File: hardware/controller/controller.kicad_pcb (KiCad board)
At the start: 4 copper layers, 59 x 47 mm, 50 parts, among them J1 Conn_01x02_Pin, J11 Barrel_Jack, J12 USB_C_Receptacle_USB2.0_14P, J2 Conn_01x02_Pin, J3 Conn_01x02_Pin, J5 Screw_Terminal_01x02, J6 Screw_Terminal_01x02, J7 Conn_01x04_Pin, J8 Conn_01x04_Pin, U1 ESP32-C3-MINI-1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

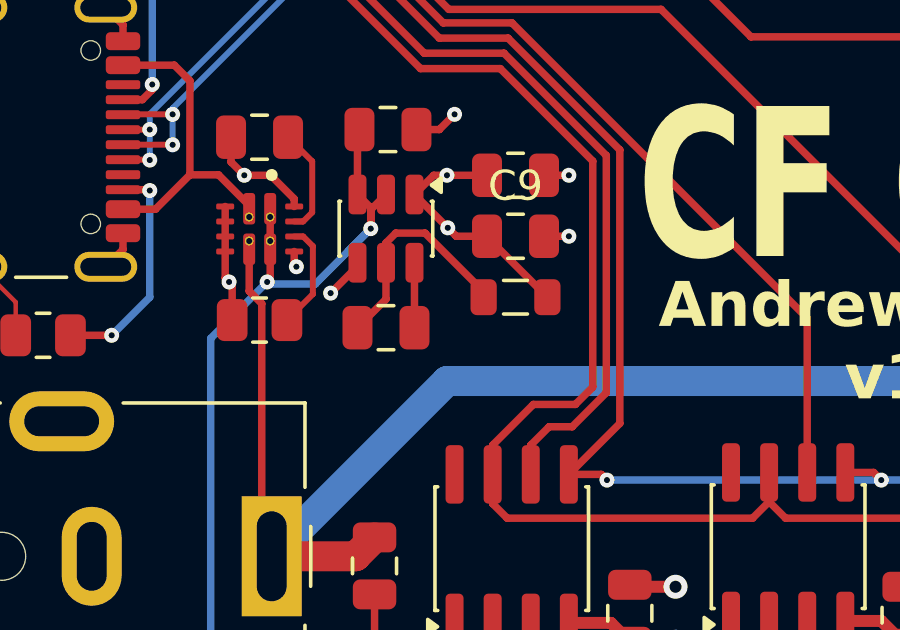
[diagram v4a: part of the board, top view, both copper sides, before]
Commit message: Update inductor to match regulator spec better
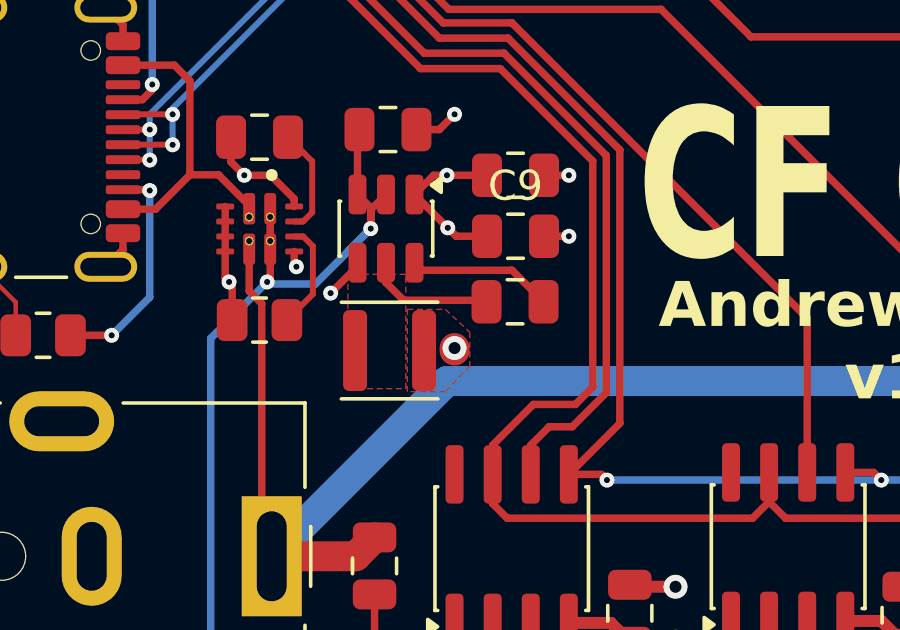
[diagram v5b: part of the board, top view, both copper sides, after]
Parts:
- L1: footprint Inductor_SMD:L_0805_2012Metric -> Inductor_SMD:L_APV_ANR3015
- moved L1 4.56 mm to (123.6, 97.3)
- moved C13 4.39 mm to (127.7, 95.7)
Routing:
- net Net-(U8-SW): track 7.60 -> 4.28 mm
- net +3V3: track 31.5 -> 28.8 mm, vias 10 -> 11
- net Net-(U8-BST): track 2.16 -> 4.84 mm
- added copper zone on F.Cu, net +3V3
- added copper zone on F.Cu, net Net-(U8-SW)
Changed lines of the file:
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@@
 	(footprint "Capacitor_SMD:C_0805_2012Metric"
 		(layer "F.Cu")
-		(at 123.444 96.52)
+		(at 127.7468 95.6564)
 		(descr "Capacitor SMD 0805 (2012 Metric), square (rectangular) end terminal, IPC-7351 nominal, (Body size source: IPC-SM-782 page 76, https://www.pcb-3d.com/wordpress/wp-content/uploads/ipc-sm-782a_amendment_1_and_2.pdf, https://docs.google.com/spreadsheets/d/1BsfQQcO9C6DZCsRaXUlFlo91Tg2WpOkGARC1WS5S8t0/edit?usp=sharing), generated with kicad-footprint-generator")
 		(tags "capacitor")
@@
 		)
 	)
-	(footprint "Inductor_SMD:L_0805_2012Metric"
+	(footprint "Inductor_SMD:L_APV_ANR3015"
 		(layer "F.Cu")
-		(at 127.762 95.504)
-		(descr "Inductor SMD 0805 (2012 Metric), square (rectangular) end terminal, IPC-7351 nominal, (Body size source: IPC-SM-782 page 80, https://www.pcb-3d.com/wordpress/wp-content/uploads/ipc-sm-782a_amendment_1_and_2.pdf), generated with kicad-footprint-generator")
-		(tags "inductor")
+		(at 123.564 97.282)
+		(descr "Inductor, APV, ANR3015, 3.0x3.0x1.5mm, (http://en.apvind.com/public/upload/20240407/3375c395e460caa8519b4d637d9113ce.pdf), generated with kicad-footprint-generator gen_inductor.py")
+		(tags "wirewound power shielded")
 		(property "Reference" "L1"
-			(at 0 -1.55 0)
+			(at 0 -2.45 0)
 			(layer "F.SilkS")
 			(hide yes)
@@
 		)
 		(property "Value" "3.9uH"
-			(at 0 1.55 0)
+			(at 0 2.45 0)
 			(layer "F.Fab")
 			(effects
@@
 			)
 		)
-		(property "LCSC" "C69486"
+		(property "LCSC" "C42429305"
 			(at 0 0 0)
 			(unlocked yes)
@@
 		(attr smd)
 		(fp_line
-			(start -0.399622 -0.56)
-			(end 0.399622 -0.56)
+			(start -1.61 -1.61)
+			(end 1.61 -1.61)
 			(stroke
 				(width 0.12)
@@
 		)
 		(fp_line
-			(start -0.399622 0.56)
-			(end 0.399622 0.56)
+			(start 1.61 1.61)
+			(end -1.61 1.61)
 			(stroke
 				(width 0.12)
@@
 		)
 		(fp_line
-			(start -1.75 -0.85)
-			(end 1.75 -0.85)
+			(start -1.8 -1.6)
+			(end -1.75 -1.6)
 			(stroke
 				(width 0.05)
@@
 		)
 		(fp_line
-			(start -1.75 0.85)
-			(end -1.75 -0.85)
+			(start -1.8 1.6)
+			(end -1.8 -1.6)
 			(stroke
 				(width 0.05)
@@
 		)
 		(fp_line
-			(start 1.75 -0.85)
-			(end 1.75 0.85)
+			(start -1.75 -1.75)
+			(end 1.75 -1.75)
 			(stroke
 				(width 0.05)
@@
 		)
 		(fp_line
-			(start 1.75 0.85)
-			(end -1.75 0.85)
+			(start -1.75 -1.6)
+			(end -1.75 -1.75)
 			(stroke
 				(width 0.05)
@@
 		)
 		(fp_line
-			(start -1 -0.45)
-			(end 1 -0.45)
+			(start -1.75 1.6)
+			(end -1.8 1.6)
 			(stroke
-				(width 0.1)
+				(width 0.05)
 				(type solid)
 			)
-			(layer "F.Fab")
+			(layer "F.CrtYd")
 		)
 		(fp_line
-			(start -1 0.45)
-			(end -1 -0.45)
+			(start -1.75 1.75)
+			(end -1.75 1.6)
 			(stroke
-				(width 0.1)
+				(width 0.05)
 				(type solid)
 			)
-			(layer "F.Fab")
+			(layer "F.CrtYd")
 		)
 		(fp_line
-			(start 1 -0.45)
-			(end 1 0.45)
+			(start 1.75 -1.75)
+			(end 1.75 -1.6)
 			(stroke
-				(width 0.1)
+				(width 0.05)
 				(type solid)
 			)
-			(layer "F.Fab")
+			(layer "F.CrtYd")
 		)
 		(fp_line
-			(start 1 0.45)
-			(end -1 0.45)
+			(start 1.75 -1.6)
+			(end 1.8 -1.6)
+			(stroke
+				(width 0.05)
+				(type solid)
+			)
+			(layer "F.CrtYd")
+		)
+		(fp_line
+			(start 1.75 1.6)
+			(end 1.75 1.75)
+			(stroke
+				(width 0.05)
+				(type solid)
+			)
+			(layer "F.CrtYd")
+		)
+		(fp_line
+			(start 1.75 1.75)
+			(end -1.75 1.75)
+			(stroke
+				(width 0.05)
+				(type solid)
+			)
+			(layer "F.CrtYd")
+		)
+		(fp_line
+			(start 1.8 -1.6)
+			(end 1.8 1.6)
+			(stroke
+				(width 0.05)
+				(type solid)
+			)
+			(layer "F.CrtYd")
+		)
+		(fp_line
+			(start 1.8 1.6)
+			(end 1.75 1.6)
+			(stroke
+				(width 0.05)
+				(type solid)
+			)
+			(layer "F.CrtYd")
+		)
+		(fp_rect
+			(start -1.5 -1.5)
+			(end 1.5 1.5)
 			(stroke
 				(width 0.1)
 				(type solid)
 			)
+			(fill no)
 			(layer "F.Fab")
 		)
@@
 			(effects
 				(font
-					(size 0.5 0.5)
-					(thickness 0.08)
+					(size 0.75 0.75)
+					(thickness 0.11)
 				)
 			)
 		)
 		(pad "1" smd roundrect
-			(at -1.0625 0)
-			(size 0.875 1.2)
+			(at -1.15 0)
+			(size 0.8 2.7)
 			(layers "F.Cu" "F.Mask" "F.Paste")
 			(roundrect_rratio 0.25)
@@
 		)
 		(pad "2" smd roundrect
-			(at 1.0625 0)
-			(size 0.875 1.2)
+			(at 1.15 0)
+			(size 0.8 2.7)
 			(layers "F.Cu" "F.Mask" "F.Paste")
 			(roundrect_rratio 0.25)
@@
 		)
 		(embedded_fonts no)
-		(model "${KICAD9_3DMODEL_DIR}/Inductor_SMD.3dshapes/L_0805_2012Metric.step"
+		(model "${KICAD9_3DMODEL_DIR}/Inductor_SMD.3dshapes/L_APV_ANR3015.step"
 			(offset
 				(xyz 0 0 0)
@@
 	)
 	(segment
-		(start 126.812 93.4915)
-		(end 128.8245 95.504)
-		(width 0.25)
-		(layer "F.Cu")
-		(net 21)
-	)
-	(segment
 		(start 126.812 93.472)
 		(end 126.812 93.4915)
@@
 		(net 21)
 	)
+	(segment
+		(start 125.73 97.282)
+		(end 125.73 97.198)
+		(width 1)
+		(layer "F.Cu")
+		(net 21)
+	)
 	(via
 		(at 110.998 78.486)
@@
 	)
 	(via
+		(at 125.73 97.198)
+		(size 0.8)
+		(drill 0.4)
+		(layers "F.Cu" "B.Cu")
+		(net 21)
+	)
+	(via
 		(at 152.146 106.934)
 		(size 0.8)
@@
 	)
 	(segment
-		(start 124.394 96.52)
+		(start 124.6439 94.6054)
 		(end 124.394 94.3555)
 		(width 0.25)
@@
 	)
 	(segment
-		(start 124.745322 93.367)
-		(end 123.770001 93.367)
-		(width 0.25)
-		(layer "F.Cu")
-		(net 56)
-	)
-	(segment
-		(start 122.494 96.52)
-		(end 123.444 95.57)
+		(start 127.6458 94.6054)
+		(end 124.6439 94.6054)
 		(width 0.25)
 		(layer "F.Cu")
-		(net 56)
+		(net 55)
 	)
 	(segment
-		(start 126.6995 95.504)
-		(end 126.6995 95.321178)
+		(start 128.6968 95.6564)
+		(end 127.6458 94.6054)
 		(width 0.25)
 		(layer "F.Cu")
-		(net 56)
+		(net 55)
 	)
 	(segment
-		(start 126.6995 95.321178)
-		(end 124.745322 93.367)
+		(start 126.7968 95.6564)
+		(end 126.7464 95.606)
 		(width 0.25)
 		(layer "F.Cu")
@@
 	)
 	(segment
-		(start 123.444 93.693001)
-		(end 123.444 94.3555)
+		(start 124.032001 95.606)
+		(end 123.444 95.017999)
 		(width 0.25)
 		(layer "F.Cu")
@@
 	)
 	(segment
-		(start 123.770001 93.367)
-		(end 123.444 93.693001)
+		(start 126.7464 95.606)
+		(end 124.032001 95.606)
 		(width 0.25)
 		(layer "F.Cu")
@@
 	)
 	(segment
-		(start 123.444 95.57)
+		(start 123.444 95.017999)
 		(end 123.444 94.3555)
 		(width 0.25)
@@
 	)
 	(zone
+		(net 21)
+		(net_name "+3V3")
+		(layer "F.Cu")
+		(hatch edge 0.5)
+		(priority 4)
+		(connect_pads yes
+			(clearance 0.5)
+		)
+		(min_thickness 0.25)
+		(filled_areas_thickness no)
+		(fill yes
+			(thermal_gap 0.5)
+			(thermal_bridge_width 0.5)
+		)
+		(polygon
+			(pts
+				(xy 124.1552 95.9104) (xy 125.4252 95.9104) (xy 126.238 96.6724) (xy 126.238 97.79) (xy 125.4252 98.6536)
+				(xy 124.1552 98.6536)
+			)
+		)
+	)
+	(zone
 		(net 18)
 		(net_name "GND")
@@
 			)
 		)
+	)
+	(zone
+		(net 56)
+		(net_name "Net-(U8-SW)")
+		(layer "F.Cu")
+		(hatch edge 0.5)
+		(priority 3)
+		(connect_pads yes
+			(clearance 0.5)
+		)
+		(min_thickness 0.25)
+		(filled_areas_thickness no)
+		(fill yes
+			(thermal_gap 0.5)
+			(thermal_bridge_width 0.5)
+		)
+		(polygon
+			(pts
+				(xy 123.19 94.742) (xy 122.174 94.742) (xy 122.174 96.012) (xy 122.174 98.552) (xy 124.1044 98.552)
+				(xy 124.1044 94.742)
+			)
+		)

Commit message: 1.1 production tweaks
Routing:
- net VBUS: track 33.1 -> 32.0 mm
- net GND: vias 47 -> 46
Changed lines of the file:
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@@
 			)
 		)
+		(property "FT Rotation Offset" "90"
+			(at 0 0 270)
+			(unlocked yes)
+			(layer "F.Fab")
+			(hide yes)
+			(effects
+				(font
+					(size 1 1)
+					(thickness 0.15)
+				)
+			)
+		)
 		(property ki_fp_filters "TSOT?23*")
 		(sheetname "/Power/")
@@
 			(at 0 -1.68 0)
 			(layer "F.SilkS")
+			(hide yes)
 			(effects
 				(font
@@
 	)
 	(via
-		(at 128.778 72.644)
-		(size 0.5)
-		(drill 0.2)
-		(layers "F.Cu" "B.Cu")
-		(net 18)
-	)
-	(via
 		(at 120.4575 94.488)
 		(size 0.5)
@@
 		(width 0.25)
 		(layer "B.Cu")
-		(net 45)
-	)
-	(segment
-		(start 122.174 93.98)
-		(end 122.936 93.218)
-		(width 0.25)
-		(layer "B.Cu")

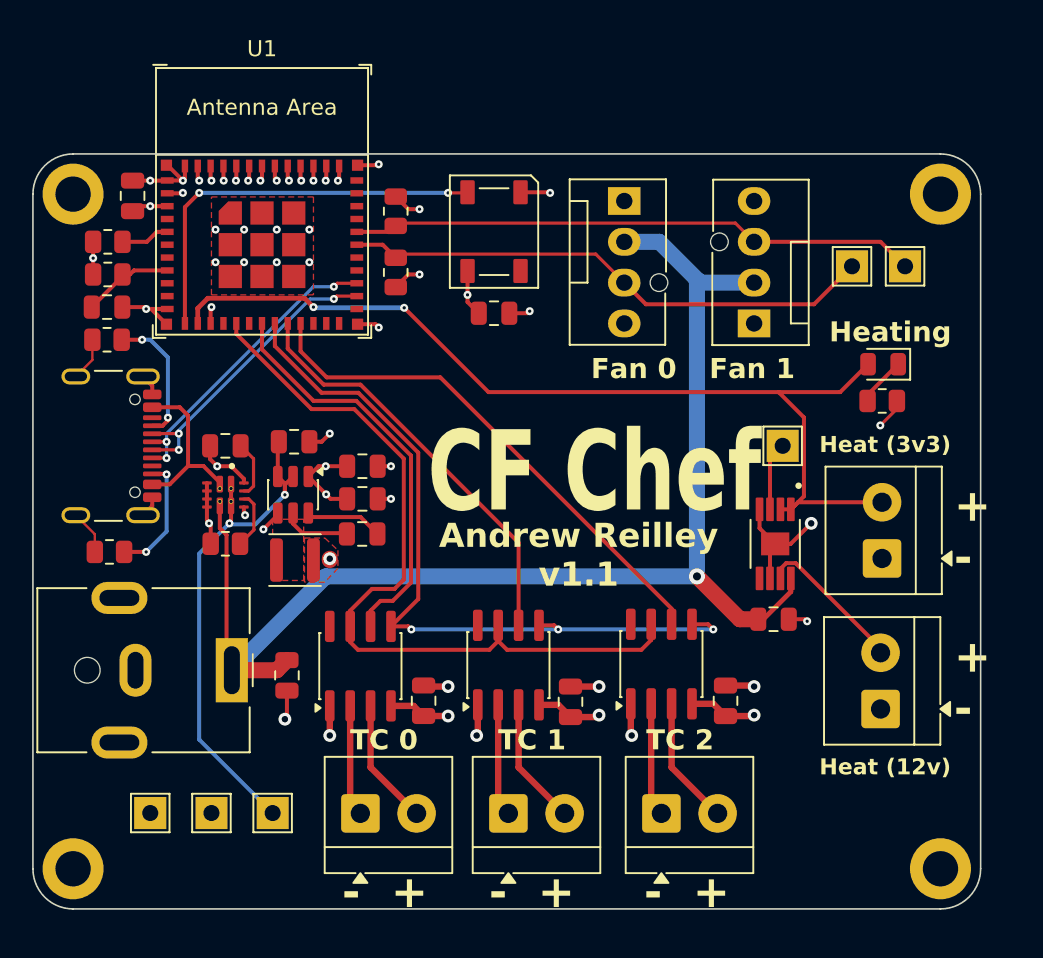
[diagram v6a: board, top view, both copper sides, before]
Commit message: Protect fan tach inputs
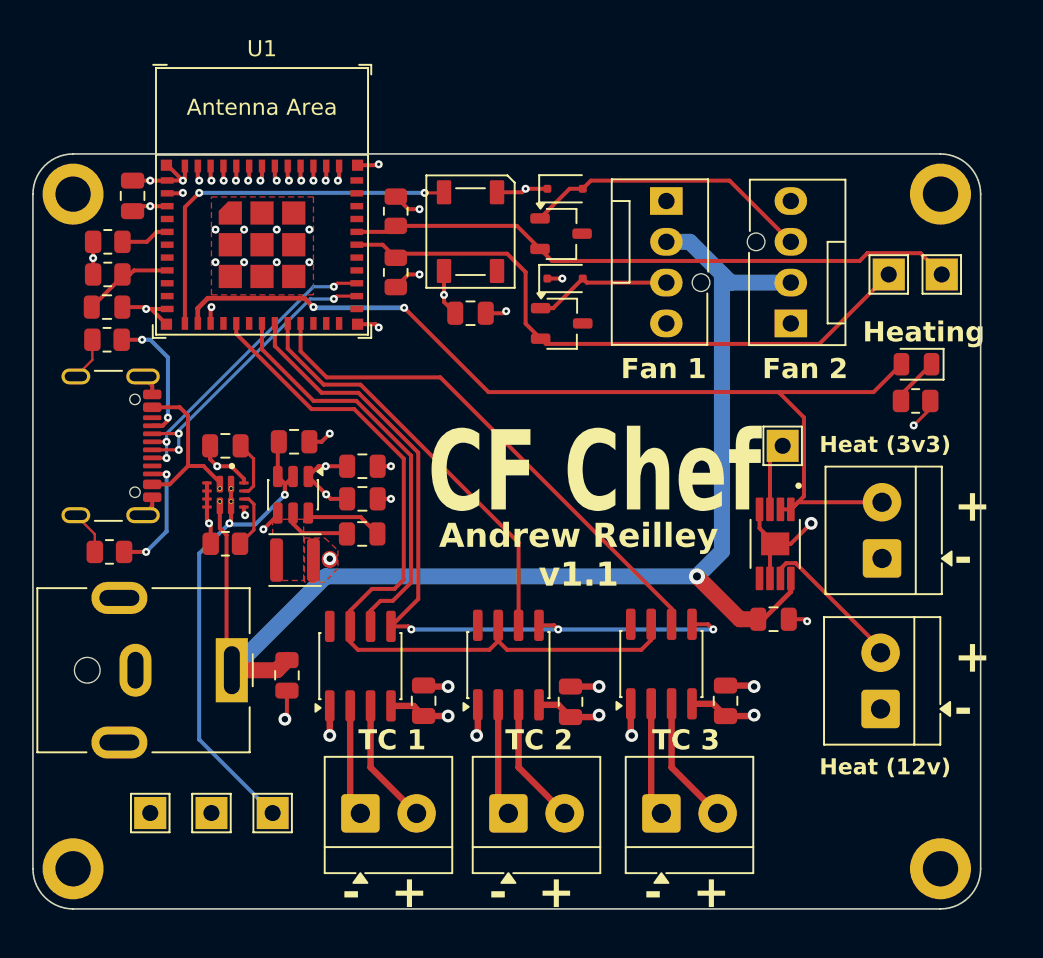
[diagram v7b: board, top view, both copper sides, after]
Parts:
- added D3: D, Package_TO_SOT_SMD:TSOT-23, F.Cu at (140.1, 77.0)
- added D4: D, Package_TO_SOT_SMD:TSOT-23, F.Cu at (140.2, 82.5)
- added D5: D_TVS, Diode_SMD:D_SOD-323F, F.Cu at (140.4, 79.8)
- added D6: D_TVS, Diode_SMD:D_SOD-323F, F.Cu at (140.4, 74.2)
- moved J7 2.62 mm to (146.7, 74.9)
- moved TP4 2.34 mm to (163.8, 79.5)
- moved TP5 2.34 mm to (160.5, 79.5)
- moved J8 2.29 mm to (154.4, 82.5)
- moved D2 2.08 mm to (162.3, 85.1)
- moved R3 2.08 mm to (162.2, 87.4)
- moved C12 1.46 mm to (134.5, 81.9)
- moved D1 1.46 mm to (134.5, 76.8)
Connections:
- R11 pad 1: FAN_0_TACH -> Net-(D4-A)
- R2 pad 1: FAN_1_TACH -> Net-(D3-A)
- TP4 pad 1: FAN_1_TACH -> Net-(D3-A)
- TP5 pad 1: FAN_0_TACH -> Net-(D4-A)
- U1 pad 30: FAN_0_TACH -> Net-(D4-A)
- U1 pad 31: FAN_1_TACH -> Net-(D3-A)
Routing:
- net Net-(D4-A): track 0.00 -> 39.9 mm
- net Net-(D3-A): track 0.00 -> 38.5 mm
- net FAN_0_TACH: track 33.9 -> 8.70 mm
- net FAN_1_TACH: track 35.5 -> 18.2 mm
- net GND: track 73.5 -> 75.8 mm, vias 46 -> 47
- net /Microcontroller/HEATER: track 60.7 -> 62.8 mm
- net /Microcontroller/LED: track 25.3 -> 23.8 mm
- net +12V: track 82.7 -> 83.3 mm
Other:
- board text added: "Fan 2"
- board text added: "TC 3"
- board text removed: "Fan 0"
- board text removed: "TC 0"

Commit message: Add TVS diode to 12V rail
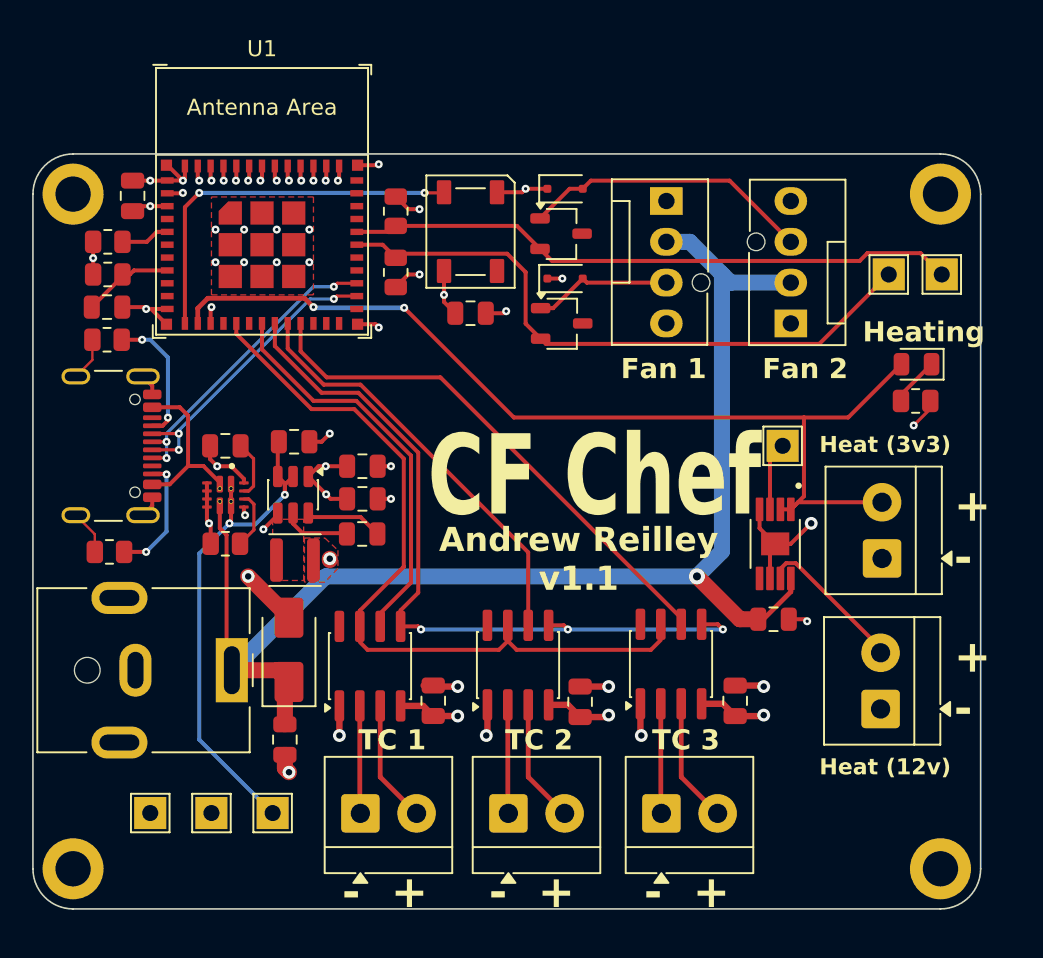
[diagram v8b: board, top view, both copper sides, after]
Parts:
- added D7: D, Diode_SMD:D_SMA, F.Cu at (123.2, 102.9)
- moved C2 4.00 mm to (122.9, 108.5)
- moved C3 0.60 mm to (151.0, 106.0)
- moved U3 0.60 mm to (137.4, 103.8)
- moved U2 0.60 mm to (128.2, 103.9)
- moved C4 0.60 mm to (132.2, 106.0)
- moved C6 0.60 mm to (141.3, 106.1)
- moved U4 0.60 mm to (147.0, 103.8)
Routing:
- net SO: track 49.9 -> 45.5 mm
- net +12V: track 83.3 -> 86.3 mm
- net GND: track 75.8 -> 78.7 mm, vias 47 -> 48
- net /Microcontroller/HEATER: track 62.8 -> 61.8 mm
- net CS0: track 25.8 -> 25.1 mm
- net Net-(J3-Pin_1): track 7.08 -> 7.73 mm
- net Net-(J2-Pin_1): track 7.02 -> 7.67 mm
- net Net-(J1-Pin_1): track 6.95 -> 7.60 mm
